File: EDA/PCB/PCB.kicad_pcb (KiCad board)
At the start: 2 copper layers, 86.4 x 53.3 mm, 12 parts, among them U1 PC817, U2 PC817, U3 PC817, U4 WeMos_D1_mini

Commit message: Update PCB
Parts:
- removed 5V_Heater1: Conn_01x01_Female, Connector_Pin:Pin_D1.3mm_L11.0mm
- added 5V_Heater: Conn_01x01_Female, Connector_Pin:Pin_D1.3mm_L11.0mm, F.Cu at (124.5, 105.4)
- renumbered 3.3V_In1 to 3.3V_In, GND_Heater1 to GND_Heater, GND_In1 to GND_In, Serial1 to Serial
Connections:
- net 0V_Stove renamed Net-(GND_Heater1-Pad1)
- net Stove_Serial renamed Net-(R3-Pad1)
- U3 pad 4: 5V_Stove -> Net-(5V_Heater1-Pad1)
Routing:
- net Net-(3.3V_In1-Pad1): track 231.5 -> 160.9 mm
- net Net-(GND_In1-Pad1): track 123.2 -> 61.3 mm
- net 5V_Stove: track 42.0 -> 0.00 mm
- net Net-(5V_Heater1-Pad1): track 0.00 -> 30.4 mm
- net Net-(R3-Pad1): track 44.1 -> 47.5 mm
- net Net-(R1-Pad2): track 18.2 -> 19.4 mm
- net Net-(U1-Pad1): track 13.6 -> 14.4 mm
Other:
- board size 86.4 x 53.3 mm -> 86.4 x 48.9 mm
- rule pad_to_mask_clearance: 0 -> 0.2
- board text added: "3.3V"
- board text added: "500"
- board text added: "GND"
- board text added: "~Ena_RX"
- board text added: "~RX"
- board text added: "~Reinit"
- board text added: "~TX"

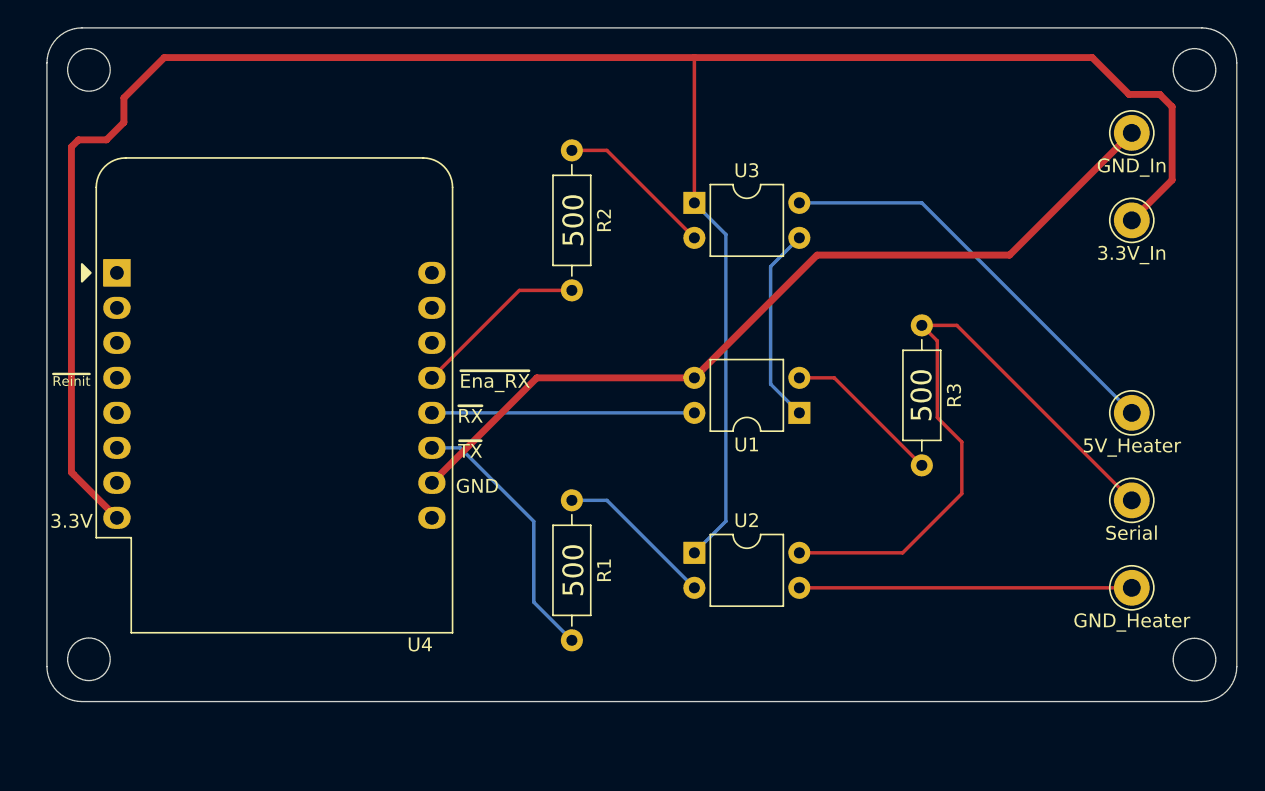
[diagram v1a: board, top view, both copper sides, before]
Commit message: Better arrangement of the traces
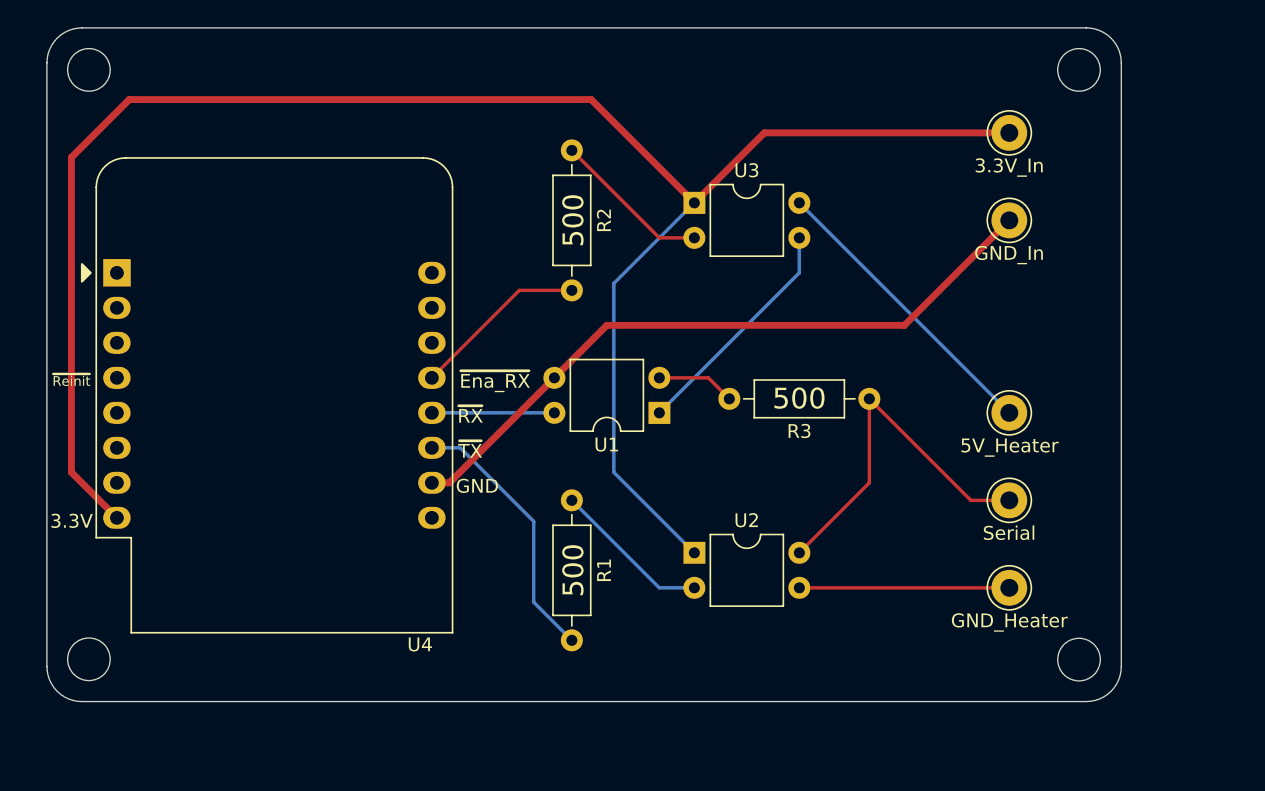
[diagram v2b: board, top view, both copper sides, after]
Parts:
- moved 3.3V_In 10.9 mm to (115.6, 85.1)
- moved GND_In 10.9 mm to (115.6, 91.4)
- moved U1 10.2 mm to (90.2, 105.4)
- moved 5V_Heater 8.89 mm to (115.6, 105.4)
- moved GND_Heater 8.89 mm to (115.6, 118.1)
- moved Serial 8.89 mm to (115.6, 111.8)
- moved R3 6.55 mm to (105.4, 104.4), turned to 180 degrees
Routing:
- net Net-(3.3V_In1-Pad1): track 160.9 -> 132.8 mm
- net Net-(R3-Pad1): track 47.5 -> 26.5 mm
- net Net-(GND_In1-Pad1): track 61.3 -> 49.8 mm
- net Net-(U1-Pad4): track 19.0 -> 8.89 mm
- net Net-(GND_Heater1-Pad1): track 24.1 -> 15.2 mm
- net Net-(5V_Heater1-Pad1): track 30.4 -> 21.6 mm
- net Net-(R3-Pad2): track 11.5 -> 5.71 mm
- net Net-(U1-Pad1): track 14.4 -> 16.9 mm
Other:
- board size 86.4 x 48.9 mm -> 78 x 48.9 mm

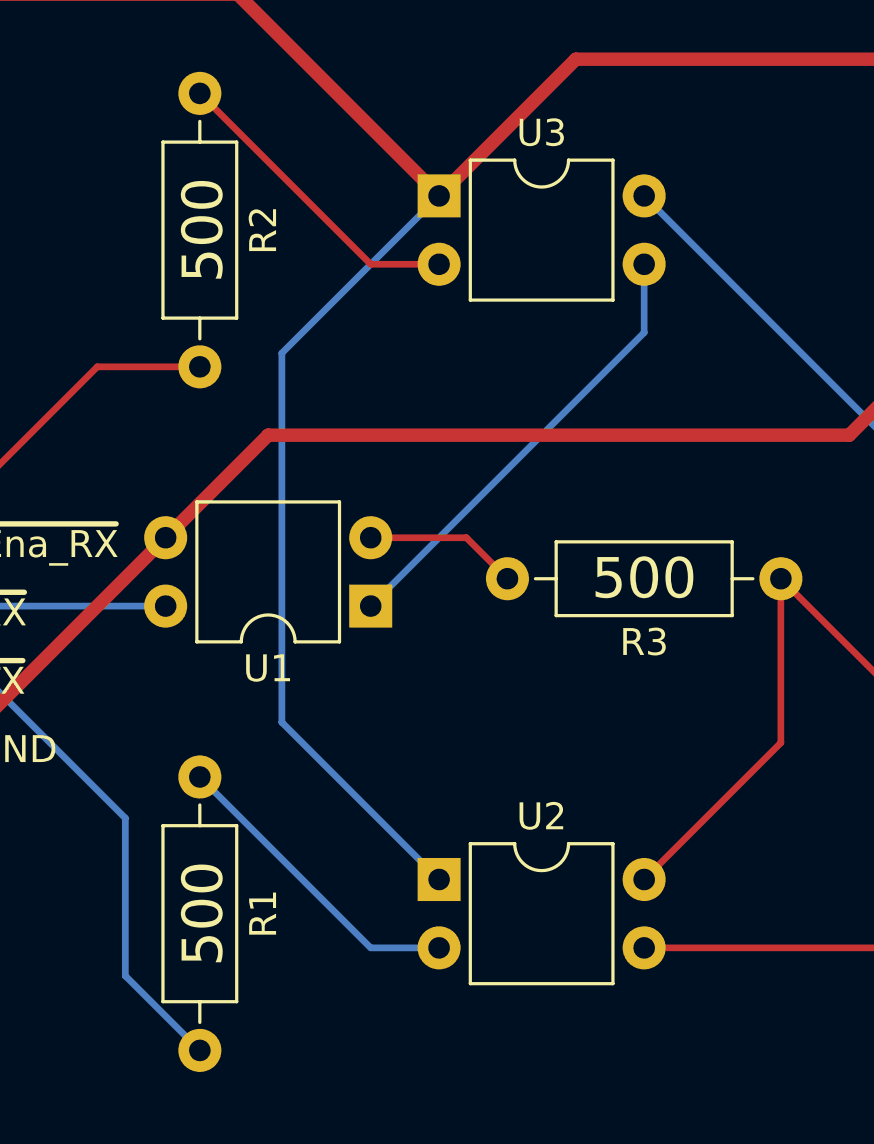
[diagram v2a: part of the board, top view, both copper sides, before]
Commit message: 500R to 510R
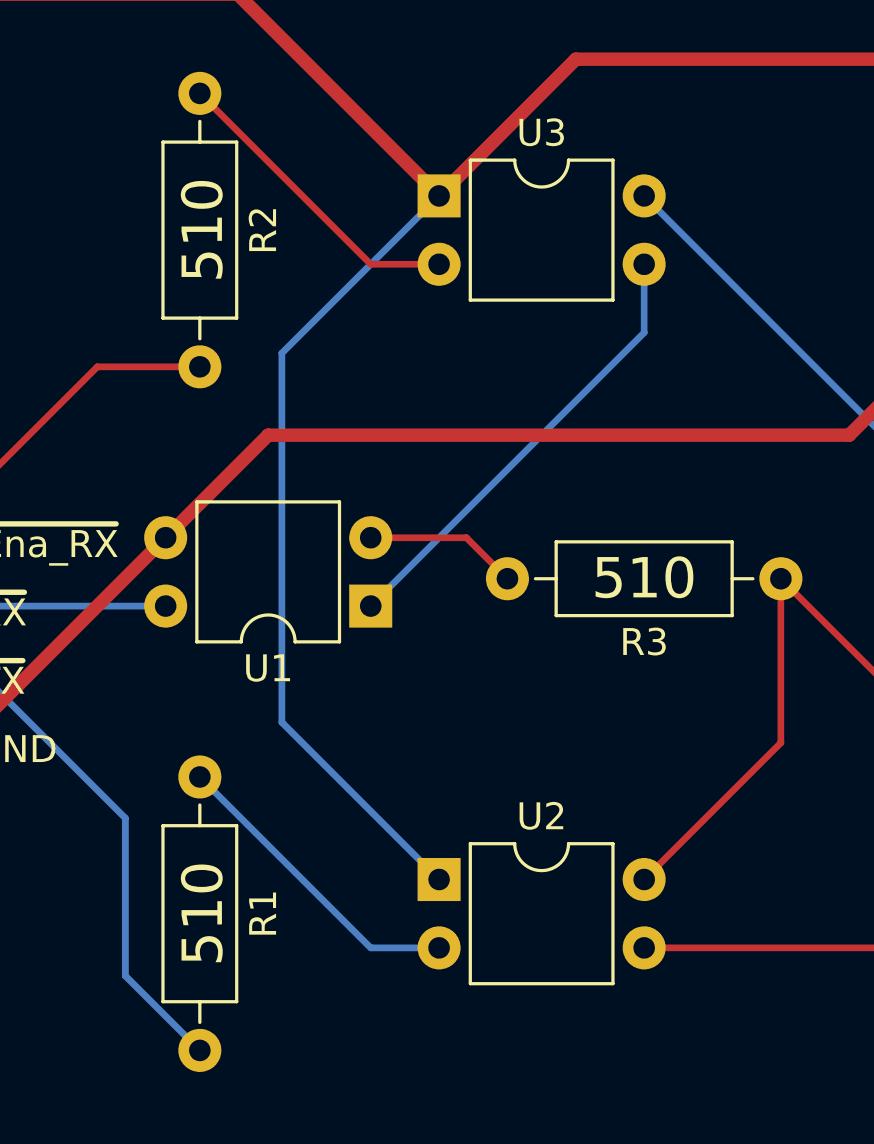
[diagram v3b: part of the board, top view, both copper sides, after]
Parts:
- R1, R2, R3: value 500 -> 510
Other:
- board text added: "510"
- board text removed: "500"
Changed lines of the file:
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@@
       (effects (font (size 1 1) (thickness 0.15)))
     )
-    (fp_text value 500 (at 5.08 2.37) (layer F.Fab)
+    (fp_text value 510 (at 5.08 2.37) (layer F.Fab)
       (effects (font (size 1 1) (thickness 0.15)))
     )
@@
       (effects (font (size 1 1) (thickness 0.15)))
     )
-    (fp_text value 500 (at 5.08 2.37 90) (layer F.Fab)
+    (fp_text value 510 (at 5.08 2.37 90) (layer F.Fab)
       (effects (font (size 1 1) (thickness 0.15)))
     )
@@
       (effects (font (size 1 1) (thickness 0.15)))
     )
-    (fp_text value 500 (at 5.08 2.37 90) (layer F.Fab)
+    (fp_text value 510 (at 5.08 2.37 90) (layer F.Fab)
       (effects (font (size 1 1) (thickness 0.15)))
     )
@@
   (gr_line (start 45.72 80.01) (end 45.72 123.825) (layer Edge.Cuts) (width 0.05))
   (gr_line (start 123.698 80.01) (end 123.698 123.825) (layer Edge.Cuts) (width 0.05))
-  (gr_text 500 (at 100.33 104.394) (layer F.SilkS)
+  (gr_text 510 (at 100.33 104.394) (layer F.SilkS)
     (effects (font (size 1.5 1.5) (thickness 0.3)))
   )
-  (gr_text 500 (at 83.947 116.84 90) (layer F.SilkS)
+  (gr_text 510 (at 83.947 116.84 90) (layer F.SilkS)
     (effects (font (size 1.5 1.5) (thickness 0.3)))
   )
-  (gr_text 500 (at 83.947 91.44 90) (layer F.SilkS)
+  (gr_text 510 (at 83.947 91.44 90) (layer F.SilkS)
     (effects (font (size 1.5 1.5) (thickness 0.3)))
   )

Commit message: Add gerber files
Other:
- rule pad_to_mask_clearance: 0.2 -> 0

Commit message: Non important PCB changes
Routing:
- net Net-(R3-Pad1): track 26.5 -> 27.2 mm

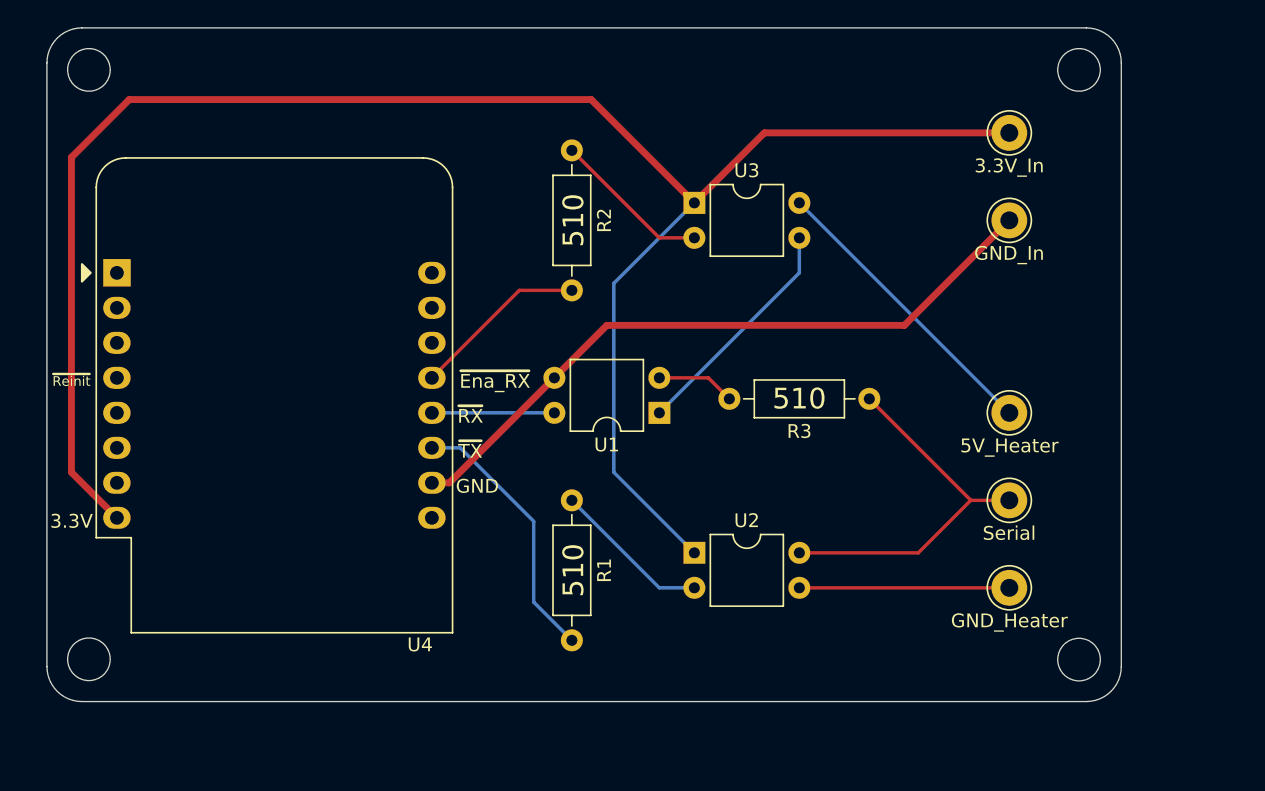
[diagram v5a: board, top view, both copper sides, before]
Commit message: Smaller PCB
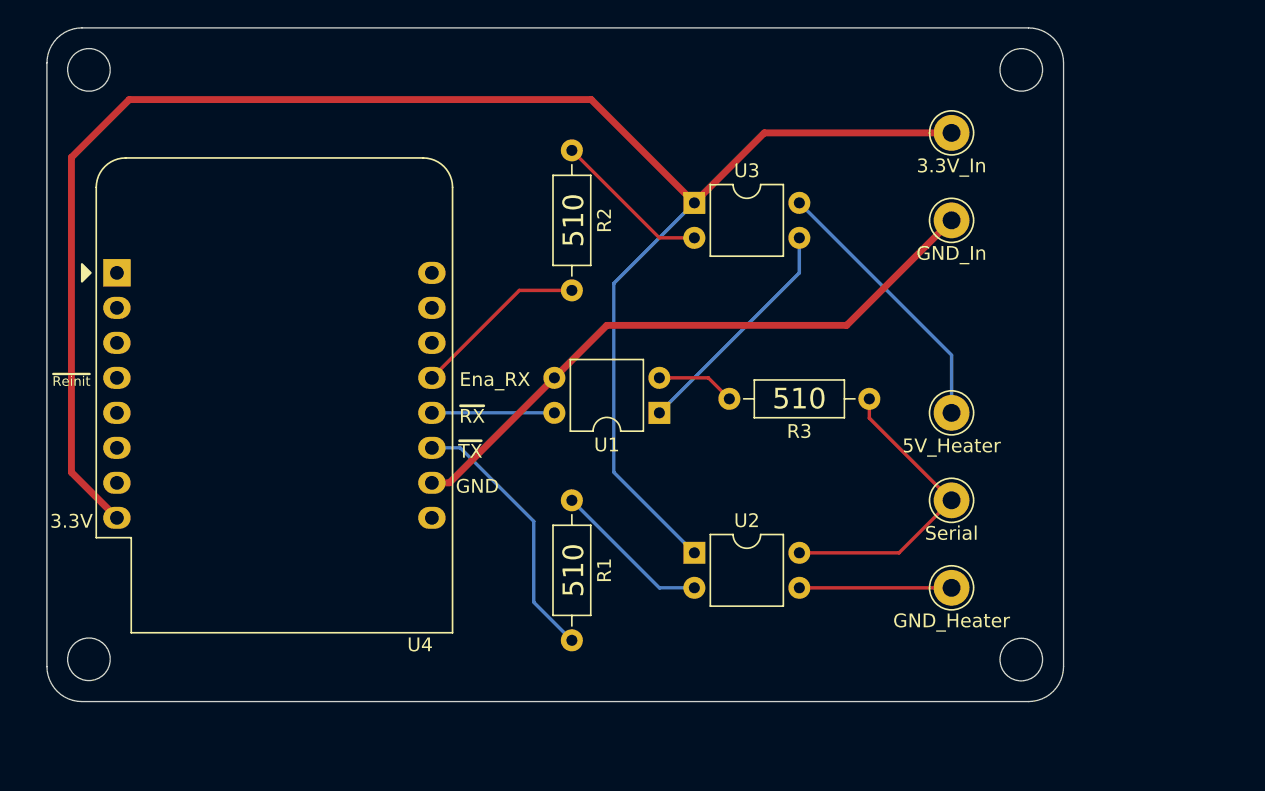
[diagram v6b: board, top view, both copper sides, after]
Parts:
- moved 3.3V_In 4.19 mm to (111.4, 85.1)
- moved 5V_Heater 4.19 mm to (111.4, 105.4)
- moved GND_Heater 4.19 mm to (111.4, 118.1)
- moved GND_In 4.19 mm to (111.4, 91.4)
- moved Serial 4.19 mm to (111.4, 111.8)
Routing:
- net Net-(R3-Pad1): track 27.2 -> 22.5 mm
- net Net-(3.3V_In1-Pad1): track 132.8 -> 128.6 mm
- net Net-(GND_In1-Pad1): track 49.8 -> 45.6 mm
- net Net-(GND_Heater1-Pad1): track 15.2 -> 11.0 mm
- net Net-(5V_Heater1-Pad1): track 21.6 -> 19.8 mm
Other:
- board size 78 x 48.9 mm -> 73.8 x 48.9 mm
- board text added: "Ena_RX"
- board text removed: "~Ena_RX"

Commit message: PCB v2
Soon on Tindie (if there are enough people interested)
https://github.com/philibertc/micronova_controller/discussions/17#discussioncomment-1496990
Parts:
- removed 3.3V_In, 5V_Heater, GND_Heater, GND_In, Serial: Conn_01x01_Female, Connector_Pin:Pin_D1.3mm_L11.0mm
- added J1: Conn_01x06_Female, Connector_PinHeader_2.54mm:PinHeader_1x06_P2.54mm_Vertical, F.Cu at (68.6, 81.5)
- added J2: Screw_Terminal_01x02, TerminalBlock:TerminalBlock_bornier-2_P5.08mm, F.Cu at (113.0, 93.7)
- added J3: Screw_Terminal_01x03, TerminalBlock:TerminalBlock_bornier-3_P5.08mm, F.Cu at (113.0, 115.6)
- added TP1: TestPoint_Flag, TestPoint:TestPoint_Pad_1.5x1.5mm, F.Cu at (80.8, 81.3)
- added TP2: TestPoint_Flag, TestPoint:TestPoint_Pad_1.5x1.5mm, F.Cu at (83.3, 81.3)
- R1: renamed from R2; value 510 -> 500
- R2: renamed from R3; value 510 -> 500
- R3: renamed from R1; value 510 -> 500
- renumbered U3 to U1, U1 to U2, U4 to U3, U2 to U4
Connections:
- U3 pad 1: Net-(U4-Pad1) -> Net-(U3-Pad1)
- U3 pad 3: Net-(U4-Pad3) -> Net-(U3-Pad1)
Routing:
- net Net-(TP1-Pad1): track 0.00 -> 55.7 mm, vias 0 -> 1
- net Net-(J2-Pad1): track 45.6 -> 91.1 mm
- net Net-(J1-Pad4): track 0.00 -> 33.2 mm
- net Net-(J1-Pad5): track 0.00 -> 29.8 mm
- net Net-(J1-Pad6): track 0.00 -> 26.0 mm
- net Net-(J1-Pad3): track 0.00 -> 23.0 mm
- net Net-(J1-Pad2): track 0.00 -> 19.4 mm
- net Net-(J1-Pad1): track 0.00 -> 15.8 mm
- net Net-(U3-Pad1): track 0.00 -> 8.93 mm
- net Net-(J2-Pad2): track 128.6 -> 131.5 mm
- net Net-(J3-Pad1): track 11.0 -> 13.8 mm
- net Net-(J3-Pad2): track 22.5 -> 24.9 mm
- net Net-(J3-Pad3): track 19.8 -> 20.5 mm
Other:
- board text added: "5V"
- board text added: "D1"
- board text added: "D6"
- board text added: "D7"
- board text added: "D8"
- board text added: "From heater"
- board text added: "PC817"
- board text added: "Power in"
- board text added: "RX"
- board text added: "Reset"
- board text added: "Serial"
- board text added: "TX"

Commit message: Update PCB.kicad_pcb
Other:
- board text added: "Reinit"
- board text removed: "Reset"
